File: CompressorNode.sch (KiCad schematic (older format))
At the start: 34 parts, among them J1 EXT1, J10 Screw_Terminal_01x03, J11 Screw_Terminal_01x02, J12 Screw_Terminal_01x03, J13 Screw_Terminal_01x04, J2 Screw_Terminal_01x04, J3 Screw_Terminal_01x03, J4 EXT2, J5 Screw_Terminal_01x02, J6 Screw_Terminal_01x02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

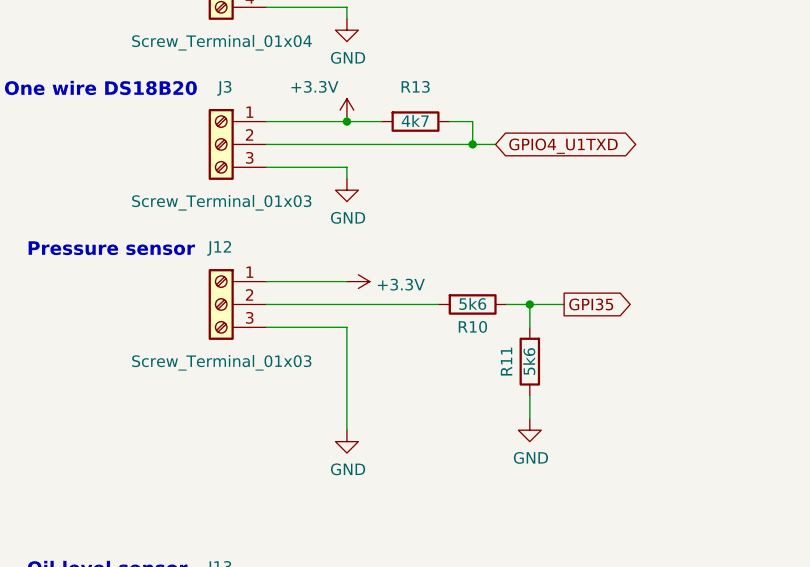
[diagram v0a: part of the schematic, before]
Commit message: Pressure sensor now connected to +5V instead of +3.3V
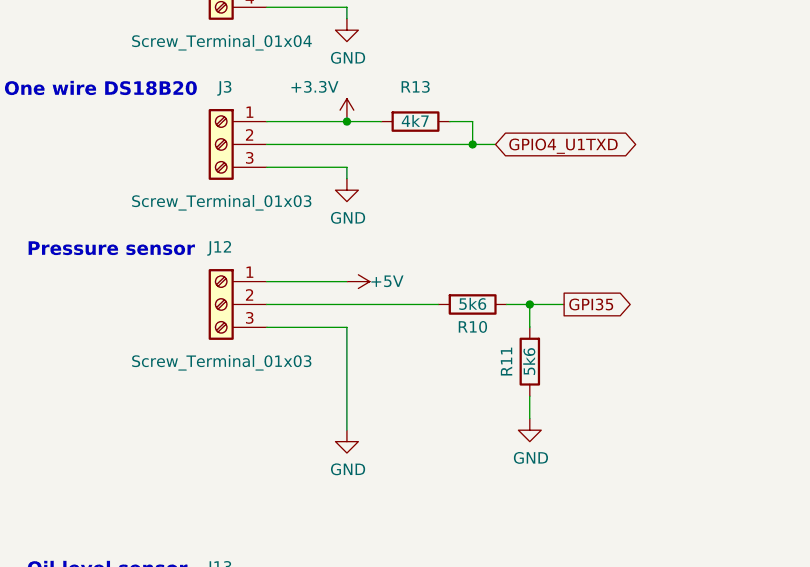
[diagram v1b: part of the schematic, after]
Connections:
- net +3V3: no longer J12.1 (Pin_1)
- net +5V: now also J12.1 (Pin_1)
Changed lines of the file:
@@
 Title "CompressorNode"
 Date "2020-04-02"
-Rev "V0.11 Concept"
+Rev "V0.12 Concept"
 Comp "MakerSpace Leiden"
 Comment1 "Getekend door Hans Beerman"
@@
 Wire Wire Line
 	2300 3950 2650 3950
-$Comp
-L power:+3.3V #PWR022
-U 1 1 5E87EA0B
-P 2650 3750
-F 0 "#PWR022" H 2650 3600 50  0001 C CNN
-F 1 "+3.3V" V 2665 3878 50  0000 L CNN
-F 2 "" H 2650 3750 50  0001 C CNN
-F 3 "" H 2650 3750 50  0001 C CNN
-	1    2650 3750
-	0    1    1    0
-$EndComp
 Wire Wire Line
 	2300 3750 2650 3750
@@
 Wire Wire Line
 	3200 3150 3300 3150
+$Comp
+L power:+5V #PWR022
+U 1 1 5E8667F5
+P 2650 3750
+F 0 "#PWR022" H 2650 3600 50  0001 C CNN
+F 1 "+5V" V 2650 3850 50  0000 L CNN
+F 2 "" H 2650 3750 50  0001 C CNN
+F 3 "" H 2650 3750 50  0001 C CNN
+	1    2650 3750
+	0    1    1    0
+$EndComp
 $EndSCHEMATC

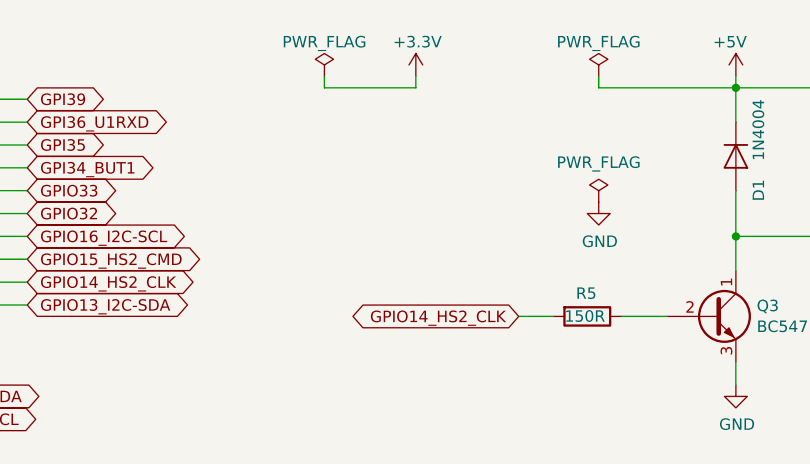
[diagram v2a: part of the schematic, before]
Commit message: Moved some screw terminals to make room for USB cable. Also added screw terminal for power (out) V0.14 Concept
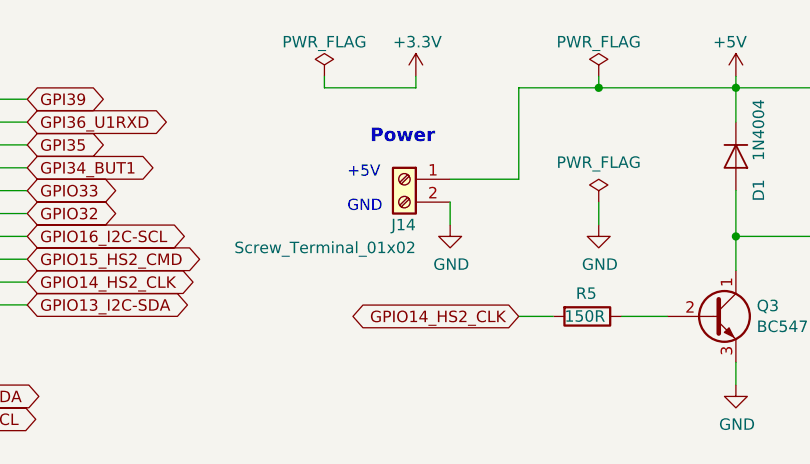
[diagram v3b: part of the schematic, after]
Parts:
- added J14: Screw_Terminal_01x02, TerminalBlock_RND:TerminalBlock_RND_205-00287_1x02_P5.08mm_Horizontal, symbol Connector:Screw_Terminal_01x02
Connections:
- net +5V: now also J14.1 (Pin_1)
- net GND: now also J14.2 (Pin_2)
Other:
- note added: "+5V"
- note added: "GND"
- note added: "Power"
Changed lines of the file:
@@
 Sheet 1 1
 Title "CompressorNode"
-Date "2020-04-04"
-Rev "V0.13 Concept"
+Date "2020-04-12"
+Rev "V0.14 Concept"
 Comp "MakerSpace Leiden"
 Comment1 "Getekend door Hans Beerman"
@@
 L power:GND #PWR013
 U 1 1 5E862388
-P 5750 1400
-F 0 "#PWR013" H 5750 1150 50  0001 C CNN
-F 1 "GND" H 5755 1227 50  0000 C CNN
-F 2 "" H 5750 1400 50  0001 C CNN
-F 3 "" H 5750 1400 50  0001 C CNN
-	1    5750 1400
+P 5750 1500
+F 0 "#PWR013" H 5750 1250 50  0001 C CNN
+F 1 "GND" H 5755 1327 50  0000 C CNN
+F 2 "" H 5750 1500 50  0001 C CNN
+F 3 "" H 5750 1500 50  0001 C CNN
+	1    5750 1500
 	1    0    0    -1
 $EndComp
@@
 	0    1    1    0
 $EndComp
+$Comp
+L Connector:Screw_Terminal_01x02 J14
+U 1 1 5E92A76E
+P 4900 1300
+F 0 "J14" H 4850 1100 50  0000 L CNN
+F 1 "Screw_Terminal_01x02" H 4850 1000 50  0000 L CNN
+F 2 "TerminalBlock_RND:TerminalBlock_RND_205-00287_1x02_P5.08mm_Horizontal" H 4900 1300 50  0001 C CNN
+F 3 "~" H 4900 1300 50  0001 C CNN
+	1    4900 1300
+	-1   0    0    -1
+$EndComp
+$Comp
+L power:GND #PWR027
+U 1 1 5E9303AE
+P 5100 1500
+F 0 "#PWR027" H 5100 1250 50  0001 C CNN
+F 1 "GND" H 5105 1327 50  0000 C CNN
+F 2 "" H 5100 1500 50  0001 C CNN
+F 3 "" H 5100 1500 50  0001 C CNN
+	1    5100 1500
+	1    0    0    -1
+$EndComp
+Wire Wire Line
+	5750 1500 5750 1400
+Wire Wire Line
+	5100 1500 5100 1400
+Wire Wire Line
+	5100 1300 5400 1300
+Wire Wire Line
+	5400 1300 5400 900
+Wire Wire Line
+	5400 900  5750 900
+Connection ~ 5750 900
+Text Notes 4650 1300 0    49   ~ 0
++5V
+Text Notes 4650 1450 0    49   ~ 0
+GND
+Text Notes 4750 1150 0    59   ~ 12
+Power
 $EndSCHEMATC

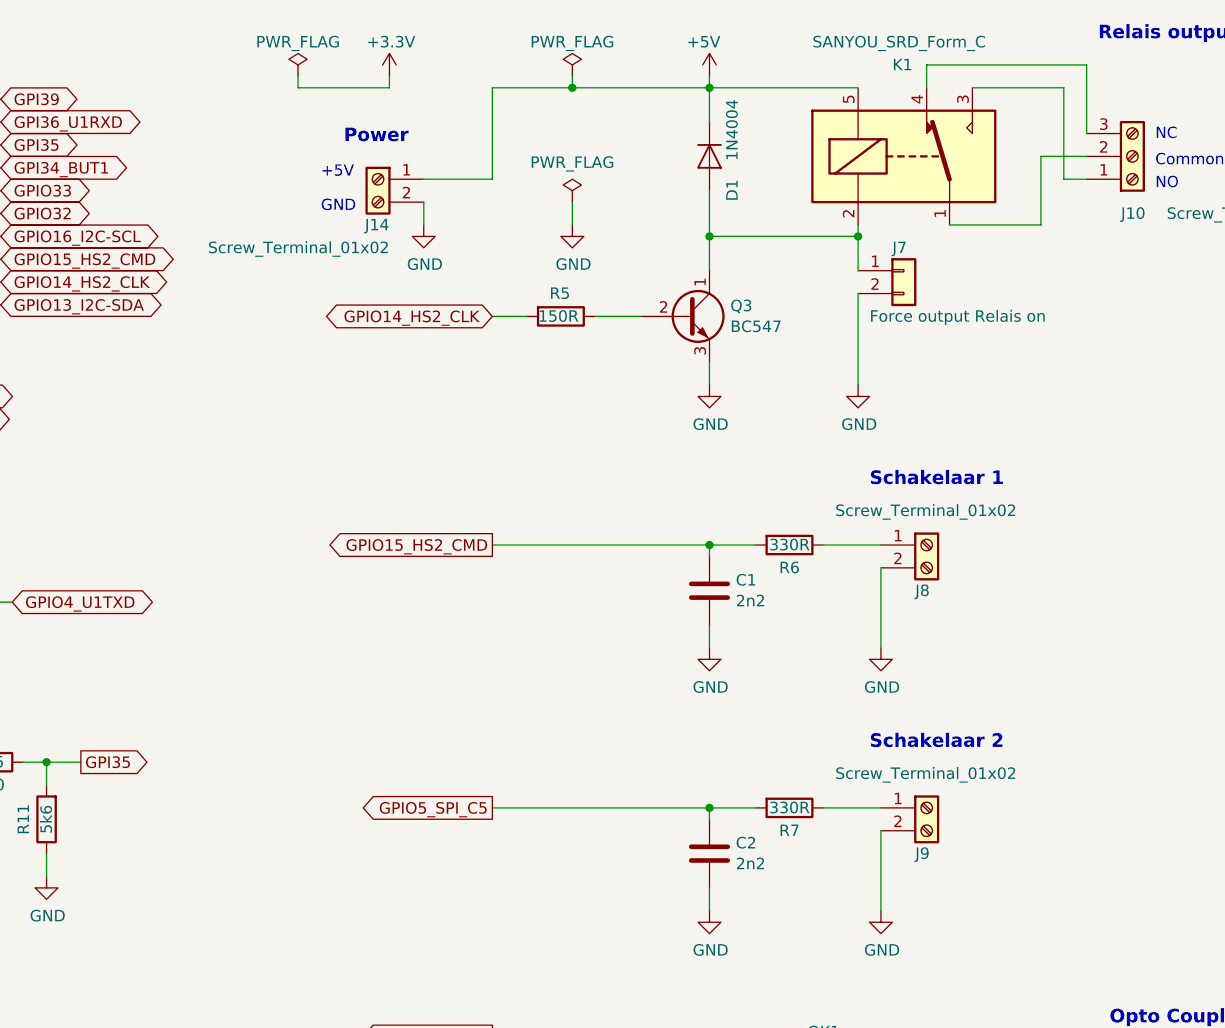
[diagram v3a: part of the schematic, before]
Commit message: Removed Power connector, added +5V output to the connectors for the switches V0.15 concept
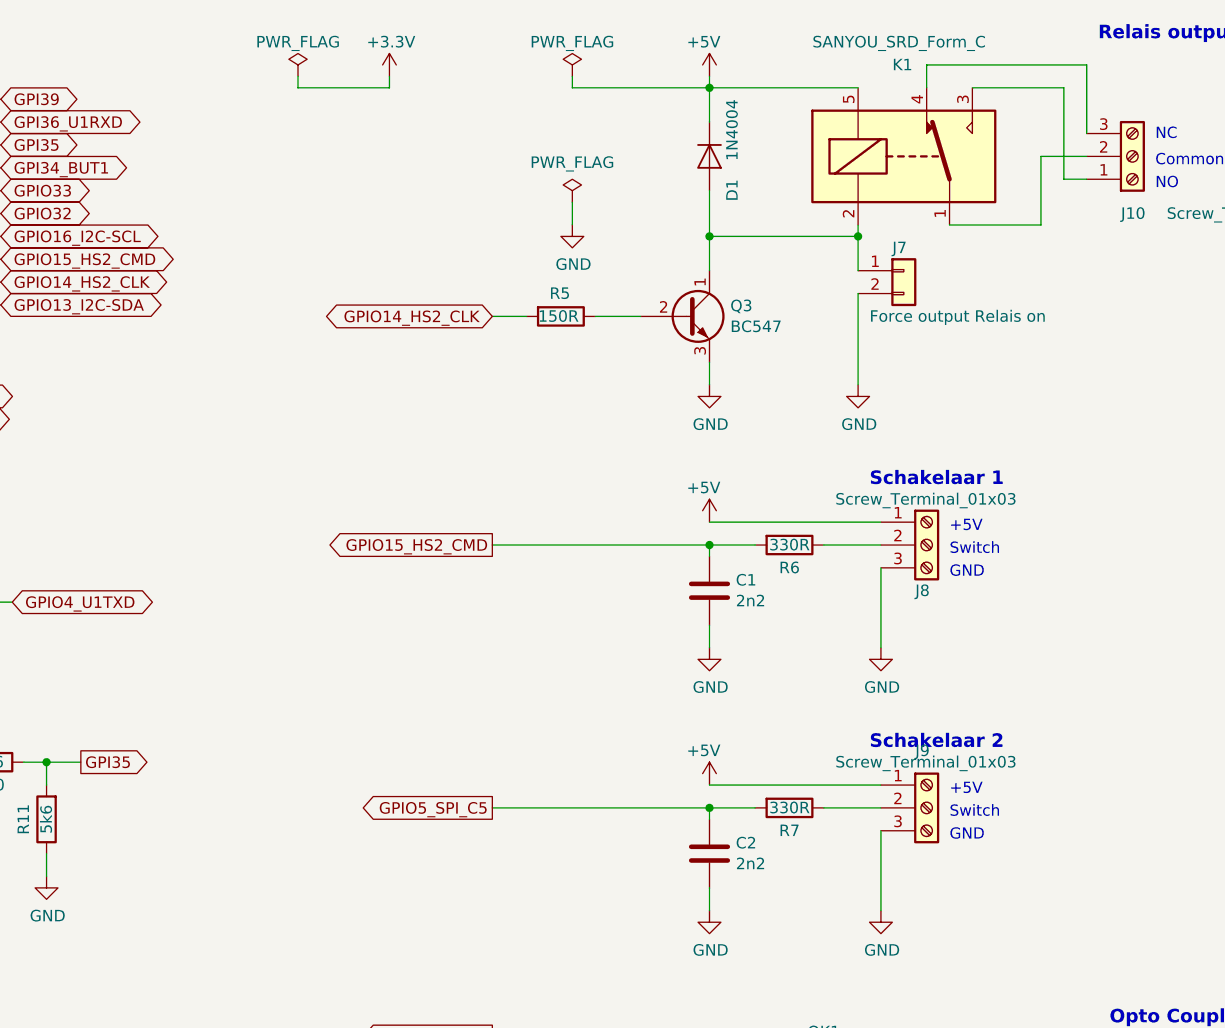
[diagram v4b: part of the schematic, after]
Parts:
- removed J14, J8, J9: Screw_Terminal_01x02, TerminalBlock_RND:TerminalBlock_RND_205-00287_1x02_P5.08mm_Horizontal, symbol Connector:Screw_Terminal_01x02
- added J8, J9: Screw_Terminal_01x03, TerminalBlock_RND:TerminalBlock_RND_205-00288_1x03_P5.08mm_Horizontal, symbol Connector:Screw_Terminal_01x03
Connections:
- net +5V: now also J8.1 (Pin_1), J9.1 (Pin_1)
- net GND: now also J8.3 (Pin_3), J9.3 (Pin_3)
- net at R6.1: now also J8.2 (Pin_2)
- net at R7.1: now also J9.2 (Pin_2)
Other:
- note added: "Switch"
- note removed: "Power"
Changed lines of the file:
@@
 Sheet 1 1
 Title "CompressorNode"
-Date "2020-04-12"
-Rev "V0.14 Concept"
+Date "2020-04-19"
+Rev "V0.15 Concept"
 Comp "MakerSpace Leiden"
 Comment1 "Getekend door Hans Beerman"
@@
 	1    0    0    -1
 $EndComp
-$Comp
-L Connector:Screw_Terminal_01x02 J8
-U 1 1 5E81ED48
-P 7300 2900
-F 0 "J8" H 7250 2700 50  0000 L CNN
-F 1 "Screw_Terminal_01x02" H 6900 3050 50  0000 L CNN
-F 2 "TerminalBlock_RND:TerminalBlock_RND_205-00287_1x02_P5.08mm_Horizontal" H 7300 2900 50  0001 C CNN
-F 3 "~" H 7300 2900 50  0001 C CNN
-	1    7300 2900
-	1    0    0    -1
-$EndComp
 Wire Wire Line
 	5400 2900 6350 2900
@@
 F 3 "" H 6350 4500 50  0001 C CNN
 	1    6350 4500
-	1    0    0    -1
-$EndComp
-$Comp
-L Connector:Screw_Terminal_01x02 J9
-U 1 1 5E82F88E
-P 7300 4050
-F 0 "J9" H 7250 3850 50  0000 L CNN
-F 1 "Screw_Terminal_01x02" H 6900 4200 50  0000 L CNN
-F 2 "TerminalBlock_RND:TerminalBlock_RND_205-00287_1x02_P5.08mm_Horizontal" H 7300 4050 50  0001 C CNN
-F 3 "~" H 7300 4050 50  0001 C CNN
-	1    7300 4050
 	1    0    0    -1
 $EndComp
@@
 	0    1    1    0
 $EndComp
-$Comp
-L Connector:Screw_Terminal_01x02 J14
-U 1 1 5E92A76E
-P 4900 1300
-F 0 "J14" H 4850 1100 50  0000 L CNN
-F 1 "Screw_Terminal_01x02" H 4850 1000 50  0000 L CNN
-F 2 "TerminalBlock_RND:TerminalBlock_RND_205-00287_1x02_P5.08mm_Horizontal" H 4900 1300 50  0001 C CNN
-F 3 "~" H 4900 1300 50  0001 C CNN
-	1    4900 1300
-	-1   0    0    -1
-$EndComp
-$Comp
-L power:GND #PWR027
-U 1 1 5E9303AE
-P 5100 1500
-F 0 "#PWR027" H 5100 1250 50  0001 C CNN
-F 1 "GND" H 5105 1327 50  0000 C CNN
-F 2 "" H 5100 1500 50  0001 C CNN
-F 3 "" H 5100 1500 50  0001 C CNN
-	1    5100 1500
-	1    0    0    -1
-$EndComp
 Wire Wire Line
 	5750 1500 5750 1400
-Wire Wire Line
-	5100 1500 5100 1400
-Wire Wire Line
-	5100 1300 5400 1300
-Wire Wire Line
-	5400 1300 5400 900
-Wire Wire Line
-	5400 900  5750 900
-Connection ~ 5750 900
-Text Notes 4650 1300 0    49   ~ 0
+Text Notes 7400 4000 0    49   ~ 0
 +5V
-Text Notes 4650 1450 0    49   ~ 0
+Text Notes 7400 4200 0    49   ~ 0
 GND
-Text Notes 4750 1150 0    59   ~ 12
-Power
+$Comp
+L Connector:Screw_Terminal_01x03 J9
+U 1 1 5E9C12F3
+P 7300 4050
+F 0 "J9" H 7250 4300 50  0000 L CNN
+F 1 "Screw_Terminal_01x03" H 6900 4250 50  0000 L CNN
+F 2 "TerminalBlock_RND:TerminalBlock_RND_205-00288_1x03_P5.08mm_Horizontal" H 7300 4050 50  0001 C CNN
+F 3 "~" H 7300 4050 50  0001 C CNN
+	1    7300 4050
+	1    0    0    -1
+$EndComp
+$Comp
+L Connector:Screw_Terminal_01x03 J8
+U 1 1 5E9C3296
+P 7300 2900
+F 0 "J8" H 7250 2700 50  0000 L CNN
+F 1 "Screw_Terminal_01x03" H 6900 3100 50  0000 L CNN
+F 2 "TerminalBlock_RND:TerminalBlock_RND_205-00288_1x03_P5.08mm_Horizontal" H 7300 2900 50  0001 C CNN
+F 3 "~" H 7300 2900 50  0001 C CNN
+	1    7300 2900
+	1    0    0    -1
+$EndComp
+$Comp
+L power:+5V #PWR027
+U 1 1 5E9D1D81
+P 6350 2800
+F 0 "#PWR027" H 6350 2650 50  0001 C CNN
+F 1 "+5V" H 6250 2950 50  0000 L CNN
+F 2 "" H 6350 2800 50  0001 C CNN
+F 3 "" H 6350 2800 50  0001 C CNN
+	1    6350 2800
+	1    0    0    -1
+$EndComp
+Wire Wire Line
+	6350 2800 7100 2800
+Text Notes 7400 4100 0    49   ~ 0
+Switch
+Text Notes 7400 2850 0    49   ~ 0
++5V
+Text Notes 7400 3050 0    49   ~ 0
+GND
+Text Notes 7400 2950 0    49   ~ 0
+Switch
+$Comp
+L power:+5V #PWR028
+U 1 1 5E9E6C83
+P 6350 3950
+F 0 "#PWR028" H 6350 3800 50  0001 C CNN
+F 1 "+5V" H 6250 4100 50  0000 L CNN
+F 2 "" H 6350 3950 50  0001 C CNN
+F 3 "" H 6350 3950 50  0001 C CNN
+	1    6350 3950
+	1    0    0    -1
+$EndComp
+Wire Wire Line
+	6350 3950 7100 3950
 $EndSCHEMATC
